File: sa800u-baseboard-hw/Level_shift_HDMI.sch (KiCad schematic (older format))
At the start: 6 parts

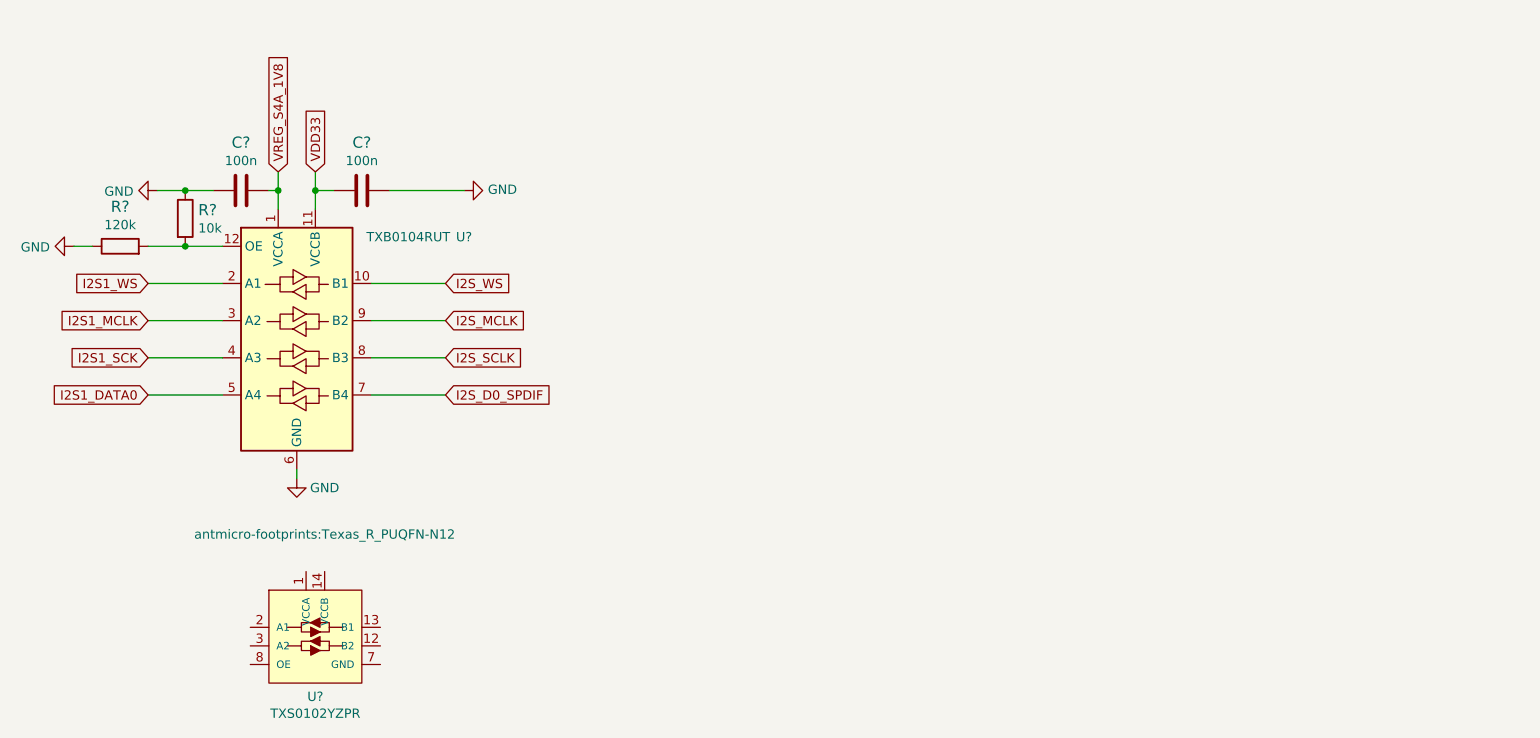
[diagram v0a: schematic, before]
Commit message: added level shifters for I2S, reset, I2C, and GPIO
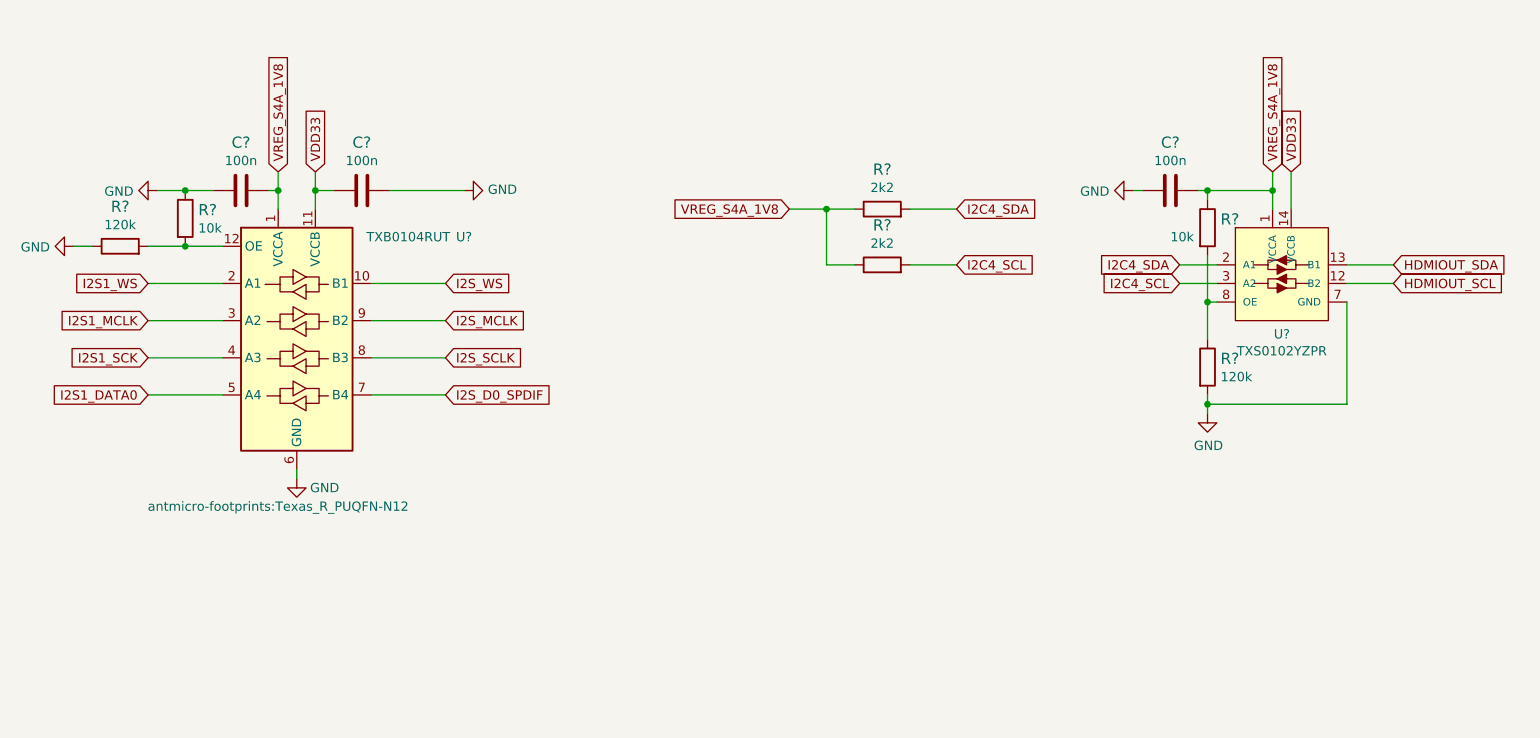
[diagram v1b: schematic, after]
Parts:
- added C?: C_100n_0402, antmicro-footprints:0402-cap, symbol antmicroCapacitors0402:C_100n_0402
- added R?: R_10k_0603, antmicro-footprints:0603-res, symbol antmicroResistors0603:R_10k_0603
- added R?: R_120k_0402, antmicro-footprints:0402-res, symbol antmicroResistors0402:R_120k_0402
- added R? (x2): R_2k2_0402, antmicro-footprints:0402-res, symbol antmicroResistors0402:R_2k2_0402
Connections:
- net GND: now also U?.7 (GND), C?.2, R?.2
- net VDD33: now also U?.14 (VCCB)
- net VREG_S4A_1V8: now also U?.1 (VCCA), C?.1, R?.1, R?.1, R?.1
- net HDMIOUT_SCL: now reaches U?.12 (B2)
- net HDMIOUT_SDA: now reaches U?.13 (B1)
- net I2C4_SDA: now reaches U?.2 (A1)
- net I2C4_SDA: now also R?.2
- net I2C4_SCL: now reaches U?.3 (A2)
- net I2C4_SCL: now also R?.2
- net at U?.8 (OE): now also R?.1, R?.2
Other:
- moved on the sheet: U?
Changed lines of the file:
@@
 F 0 "U?" H 4650 3100 50  0000 C CNN
 F 1 "TXB0104RUT" H 4350 3100 50  0000 C CNN
-F 2 "antmicro-footprints:Texas_R_PUQFN-N12" H 3900 1500 50  0000 C CNN
+F 2 "antmicro-footprints:Texas_R_PUQFN-N12" H 3650 1650 50  0000 C CNN
 F 3 "http://www.ti.com/lit/ds/symlink/txb0104.pdf" H 3860 2645 50  0001 C CNN
 F 4 "Texas Instruments" H 3350 1700 50  0001 C CNN "Manufacturer"
@@
 L HDMI:TXS0102YZPR U?
 U 1 1 61AE6E30
-P 3600 3900
-F 0 "U?" H 3850 3327 50  0000 C CNN
-F 1 "TXS0102YZPR" H 3850 3236 50  0000 C CNN
-F 2 "" H 3050 4100 50  0001 C CNN
-F 3 "" H 3050 4100 50  0001 C CNN
-	1    3600 3900
+P 8800 1950
+F 0 "U?" H 9050 1377 50  0000 C CNN
+F 1 "TXS0102YZPR" H 9050 1286 50  0000 C CNN
+F 2 "" H 8250 2150 50  0001 C CNN
+F 3 "" H 8250 2150 50  0001 C CNN
+	1    8800 1950
 	1    0    0    -1
 $EndComp
@@
 Wire Wire Line
 	3750 3300 3750 3250
+Text GLabel 8500 2250 0    50   Input ~ 0
+I2C4_SCL
+Text GLabel 9650 2250 2    50   Input ~ 0
+HDMIOUT_SCL
+Text GLabel 8500 2150 0    50   Input ~ 0
+I2C4_SDA
+Text GLabel 9650 2150 2    50   Input ~ 0
+HDMIOUT_SDA
+Wire Wire Line
+	8700 2150 8500 2150
+Wire Wire Line
+	8500 2250 8700 2250
+Wire Wire Line
+	9400 2150 9650 2150
+Wire Wire Line
+	9400 2250 9650 2250
+Text GLabel 9000 1650 1    50   Input ~ 0
+VREG_S4A_1V8
+Text GLabel 9100 1650 1    50   Input ~ 0
+VDD33
+Wire Wire Line
+	9000 1650 9000 1750
+Wire Wire Line
+	9100 1650 9100 1850
+Wire Wire Line
+	9000 1750 8650 1750
+Connection ~ 9000 1750
+Wire Wire Line
+	9000 1750 9000 1850
+$Comp
+L antmicroCapacitors0402:C_100n_0402 C?
+U 1 1 61B0A89F
+P 8450 1750
+F 0 "C?" V 8192 1750 60  0000 C CNN
+F 1 "C_100n_0402" H 8450 1600 60  0001 C CNN
+F 2 "antmicro-footprints:0402-cap" H 8650 1950 60  0001 L CNN
+F 3 "" H 8450 1750 50  0001 C CNN
+F 4 "Walsin" H 8650 2150 60  0001 L CNN "Manufacturer"
+F 5 "0402X104K6R3CT" H 8650 2050 60  0001 L CNN "MPN"
+F 6 "100n" V 8290 1750 50  0000 C CNN "Val"
+	1    8450 1750
+	0    1    1    0
+$EndComp
+Wire Wire Line
+	8300 1750 8250 1750
+$Comp
+L power:GND #PWR?
+U 1 1 61B0B3E9
+P 8250 1750
+F 0 "#PWR?" H 8250 1500 50  0001 C CNN
+F 1 "GND" V 8255 1622 50  0000 R CNN
+F 2 "" H 8250 1750 50  0001 C CNN
+F 3 "" H 8250 1750 50  0001 C CNN
+	1    8250 1750
+	0    1    1    0
+$EndComp
+Wire Wire Line
+	8650 1750 8650 1800
+Wire Wire Line
+	8650 2350 8700 2350
+Connection ~ 8650 1750
+Wire Wire Line
+	8650 1750 8600 1750
+Wire Wire Line
+	8650 2350 8650 2550
+Connection ~ 8650 2350
+$Comp
+L antmicroResistors0603:R_10k_0603 R?
+U 1 1 61B0D538
+P 8650 1950
+F 0 "R?" V 8605 2020 60  0000 L CNN
+F 1 "R_10k_0603" H 8650 1800 60  0001 C CNN
+F 2 "antmicro-footprints:0603-res" H 8850 2150 60  0001 L CNN
+F 3 "" H 8650 1950 50  0001 C CNN
+F 4 "BOURNS" H 8850 2350 60  0001 L CNN "Manufacturer"
+F 5 "CR0603-JW-103ELF" H 8850 2250 60  0001 L CNN "MPN"
+F 6 "10k" V 8700 1750 50  0000 L CNN "Val"
+	1    8650 1950
+	0    1    1    0
+$EndComp
+Wire Wire Line
+	8650 2100 8650 2350
+$Comp
+L antmicroResistors0402:R_120k_0402 R?
+U 1 1 61B0E0A9
+P 8650 2700
+F 0 "R?" V 8605 2770 60  0000 L CNN
+F 1 "R_120k_0402" H 8650 2550 60  0001 C CNN
+F 2 "antmicro-footprints:0402-res" H 8850 2900 60  0001 L CNN
+F 3 "" H 8650 2700 50  0001 C CNN
+F 4 "VISHAY" H 8850 3100 60  0001 L CNN "Manufacturer"
+F 5 "CRCW0402120KFKED" H 8850 3000 60  0001 L CNN "MPN"
+F 6 "120k" V 8703 2770 50  0000 L CNN "Val"
+	1    8650 2700
+	0    1    1    0
+$EndComp
+$Comp
+L power:GND #PWR?
+U 1 1 61B0EB2E
+P 8650 2950
+F 0 "#PWR?" H 8650 2700 50  0001 C CNN
+F 1 "GND" H 8655 2777 50  0000 C CNN
+F 2 "" H 8650 2950 50  0001 C CNN
+F 3 "" H 8650 2950 50  0001 C CNN
+	1    8650 2950
+	1    0    0    -1
+$EndComp
+Wire Wire Line
+	8650 2950 8650 2900
+Wire Wire Line
+	9400 2350 9400 2900
+Wire Wire Line
+	9400 2900 8650 2900
+Connection ~ 8650 2900
+Wire Wire Line
+	8650 2900 8650 2850
+$Comp
+L antmicroResistors0402:R_2k2_0402 R?
+U 1 1 61B1457B
+P 6900 1850
+F 0 "R?" H 6900 2063 60  0000 C CNN
+F 1 "R_2k2_0402" H 6900 1700 60  0001 C CNN
+F 2 "antmicro-footprints:0402-res" H 7100 2050 60  0001 L CNN
+F 3 "" H 6900 1850 50  0001 C CNN
+F 4 "YAGEO" H 7100 2250 60  0001 L CNN "Manufacturer"
+F 5 "RC0402FR-072K2L" H 7100 2150 60  0001 L CNN "MPN"
+F 6 "2k2" H 6900 1965 50  0000 C CNN "Val"
+	1    6900 1850
+	1    0    0    -1
+$EndComp
+$Comp
+L antmicroResistors0402:R_2k2_0402 R?
+U 1 1 61B14A5A
+P 6900 2150
+F 0 "R?" H 6900 2363 60  0000 C CNN
+F 1 "R_2k2_0402" H 6900 2000 60  0001 C CNN
+F 2 "antmicro-footprints:0402-res" H 7100 2350 60  0001 L CNN
+F 3 "" H 6900 2150 50  0001 C CNN
+F 4 "YAGEO" H 7100 2550 60  0001 L CNN "Manufacturer"
+F 5 "RC0402FR-072K2L" H 7100 2450 60  0001 L CNN "MPN"
+F 6 "2k2" H 6900 2265 50  0000 C CNN "Val"
+	1    6900 2150
+	1    0    0    -1
+$EndComp
+Wire Wire Line
+	6750 1850 6600 1850
+Wire Wire Line
+	6750 2150 6600 2150
+Wire Wire Line
+	6600 2150 6600 1850
+Connection ~ 6600 1850
+Wire Wire Line
+	6600 1850 6400 1850
+Text GLabel 6400 1850 0    50   Input ~ 0
+VREG_S4A_1V8
+Text GLabel 7300 1850 2    50   Input ~ 0
+I2C4_SDA
+Text GLabel 7300 2150 2    50   Input ~ 0
+I2C4_SCL
+Wire Wire Line
+	7050 1850 7300 1850
+Wire Wire Line
+	7050 2150 7300 2150
 $EndSCHEMATC

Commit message: Review - Add geeral remarks
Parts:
- gave numbers to parts that had none: 11
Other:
- note added: "REMARK:Please unify convention of naming power supply labels.\nWe often use global labels. Always check that the name is exactly the same."
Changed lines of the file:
@@
 $EndDescr
 $Comp
-L antmicroLogicTranslatorsLevelShifters:TXB0104RUT U?
+L antmicroLogicTranslatorsLevelShifters:TXB0104RUT U5
 U 1 1 61AD2A25
 P 3750 2550
-F 0 "U?" H 4650 3100 50  0000 C CNN
+F 0 "U5" H 4650 3100 50  0000 C CNN
 F 1 "TXB0104RUT" H 4350 3100 50  0000 C CNN
 F 2 "antmicro-footprints:Texas_R_PUQFN-N12" H 3650 1650 50  0000 C CNN
@@
 I2S1_DATA0
 $Comp
-L HDMI:TXS0102YZPR U?
+L HDMI:TXS0102YZPR U6
 U 1 1 61AE6E30
 P 8800 1950
-F 0 "U?" H 9050 1377 50  0000 C CNN
+F 0 "U6" H 9050 1377 50  0000 C CNN
 F 1 "TXS0102YZPR" H 9050 1286 50  0000 C CNN
 F 2 "" H 8250 2150 50  0001 C CNN
@@
 	4150 2250 4550 2250
 $Comp
-L power:GND #PWR?
+L power:GND #PWR0119
 U 1 1 61AEC03D
 P 3000 1750
-F 0 "#PWR?" H 3000 1500 50  0001 C CNN
+F 0 "#PWR0119" H 3000 1500 50  0001 C CNN
 F 1 "GND" V 3005 1622 50  0000 R CNN
 F 2 "" H 3000 1750 50  0001 C CNN
@@
 	3650 1750 3650 1850
 $Comp
-L power:GND #PWR?
+L power:GND #PWR0120
 U 1 1 61AEC562
 P 4650 1750
-F 0 "#PWR?" H 4650 1500 50  0001 C CNN
+F 0 "#PWR0120" H 4650 1500 50  0001 C CNN
 F 1 "GND" V 4655 1622 50  0000 R CNN
 F 2 "" H 4650 1750 50  0001 C CNN
@@
 	3850 1750 3850 1850
 $Comp
-L antmicroCapacitors0402:C_100n_0402 C?
+L antmicroCapacitors0402:C_100n_0402 C34
 U 1 1 61AEDF92
 P 3450 1750
-F 0 "C?" V 3192 1750 60  0000 C CNN
+F 0 "C34" V 3192 1750 60  0000 C CNN
 F 1 "C_100n_0402" H 3450 1600 60  0001 C CNN
 F 2 "antmicro-footprints:0402-cap" H 3650 1950 60  0001 L CNN
@@
 	3600 1750 3650 1750
 $Comp
-L antmicroCapacitors0402:C_100n_0402 C?
+L antmicroCapacitors0402:C_100n_0402 C35
 U 1 1 61AEE5E6
 P 4100 1750
-F 0 "C?" V 3842 1750 60  0000 C CNN
+F 0 "C35" V 3842 1750 60  0000 C CNN
 F 1 "C_100n_0402" H 4100 1600 60  0001 C CNN
 F 2 "antmicro-footprints:0402-cap" H 4300 1950 60  0001 L CNN
@@
 	3350 2050 3150 2050
 $Comp
-L antmicroResistors0603:R_10k_0603 R?
+L antmicroResistors0603:R_10k_0603 R45
 U 1 1 61AF1E74
 P 3150 1900
-F 0 "R?" V 3105 1970 60  0000 L CNN
+F 0 "R45" V 3105 1970 60  0000 L CNN
 F 1 "R_10k_0603" H 3150 1750 60  0001 C CNN
 F 2 "antmicro-footprints:0603-res" H 3350 2100 60  0001 L CNN
@@
 	3150 2050 2950 2050
 $Comp
-L antmicroResistors0402:R_120k_0402 R?
+L antmicroResistors0402:R_120k_0402 R44
 U 1 1 61AF2C4D
 P 2800 2050
-F 0 "R?" H 2800 2263 60  0000 C CNN
+F 0 "R44" H 2800 2263 60  0000 C CNN
 F 1 "R_120k_0402" H 2800 1900 60  0001 C CNN
 F 2 "antmicro-footprints:0402-res" H 3000 2250 60  0001 L CNN
@@
 $EndComp
 $Comp
-L power:GND #PWR?
+L power:GND #PWR0121
 U 1 1 61AF30FD
 P 2550 2050
-F 0 "#PWR?" H 2550 1800 50  0001 C CNN
+F 0 "#PWR0121" H 2550 1800 50  0001 C CNN
 F 1 "GND" V 2555 1922 50  0000 R CNN
 F 2 "" H 2550 2050 50  0001 C CNN
@@
 	2550 2050 2650 2050
 $Comp
-L power:GND #PWR?
+L power:GND #PWR0122
 U 1 1 61AF391A
 P 3750 3300
-F 0 "#PWR?" H 3750 3050 50  0001 C CNN
+F 0 "#PWR0122" H 3750 3050 50  0001 C CNN
 F 1 "GND" H 3900 3250 50  0000 C CNN
 F 2 "" H 3750 3300 50  0001 C CNN
@@
 	9000 1750 9000 1850
 $Comp
-L antmicroCapacitors0402:C_100n_0402 C?
+L antmicroCapacitors0402:C_100n_0402 C36
 U 1 1 61B0A89F
 P 8450 1750
-F 0 "C?" V 8192 1750 60  0000 C CNN
+F 0 "C36" V 8192 1750 60  0000 C CNN
 F 1 "C_100n_0402" H 8450 1600 60  0001 C CNN
 F 2 "antmicro-footprints:0402-cap" H 8650 1950 60  0001 L CNN
@@
 	8300 1750 8250 1750
 $Comp
-L power:GND #PWR?
+L power:GND #PWR0123
 U 1 1 61B0B3E9
 P 8250 1750
-F 0 "#PWR?" H 8250 1500 50  0001 C CNN
+F 0 "#PWR0123" H 8250 1500 50  0001 C CNN
 F 1 "GND" V 8255 1622 50  0000 R CNN
 F 2 "" H 8250 1750 50  0001 C CNN
@@
 Connection ~ 8650 2350
 $Comp
-L antmicroResistors0603:R_10k_0603 R?
+L antmicroResistors0603:R_10k_0603 R48
 U 1 1 61B0D538
 P 8650 1950
-F 0 "R?" V 8605 2020 60  0000 L CNN
+F 0 "R48" V 8605 2020 60  0000 L CNN
 F 1 "R_10k_0603" H 8650 1800 60  0001 C CNN
 F 2 "antmicro-footprints:0603-res" H 8850 2150 60  0001 L CNN
@@
 	8650 2100 8650 2350
 $Comp
-L antmicroResistors0402:R_120k_0402 R?
+L antmicroResistors0402:R_120k_0402 R49
 U 1 1 61B0E0A9
 P 8650 2700
-F 0 "R?" V 8605 2770 60  0000 L CNN
+F 0 "R49" V 8605 2770 60  0000 L CNN
 F 1 "R_120k_0402" H 8650 2550 60  0001 C CNN
 F 2 "antmicro-footprints:0402-res" H 8850 2900 60  0001 L CNN
@@
 $EndComp
 $Comp
-L power:GND #PWR?
+L power:GND #PWR0124
 U 1 1 61B0EB2E
 P 8650 2950
-F 0 "#PWR?" H 8650 2700 50  0001 C CNN
+F 0 "#PWR0124" H 8650 2700 50  0001 C CNN
 F 1 "GND" H 8655 2777 50  0000 C CNN
 F 2 "" H 8650 2950 50  0001 C CNN
@@
 	8650 2900 8650 2850
 $Comp
-L antmicroResistors0402:R_2k2_0402 R?
+L antmicroResistors0402:R_2k2_0402 R46
 U 1 1 61B1457B
 P 6900 1850
-F 0 "R?" H 6900 2063 60  0000 C CNN
+F 0 "R46" H 6900 2063 60  0000 C CNN
 F 1 "R_2k2_0402" H 6900 1700 60  0001 C CNN
 F 2 "antmicro-footprints:0402-res" H 7100 2050 60  0001 L CNN
@@
 $EndComp
 $Comp
-L antmicroResistors0402:R_2k2_0402 R?
+L antmicroResistors0402:R_2k2_0402 R47
 U 1 1 61B14A5A
 P 6900 2150
-F 0 "R?" H 6900 2363 60  0000 C CNN
+F 0 "R47" H 6900 2363 60  0000 C CNN
 F 1 "R_2k2_0402" H 6900 2000 60  0001 C CNN
 F 2 "antmicro-footprints:0402-res" H 7100 2350 60  0001 L CNN
@@
 Wire Wire Line
 	7050 2150 7300 2150
+Text Notes 3650 975  0    50   ~ 0
+REMARK:Please unify convention of naming power supply labels.\nWe often use global labels. Always check that the name is exactly the same.
 $EndSCHEMATC

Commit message: introducing minor genreal improvements
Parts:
- removed U6: TXS0102YZPR, symbol HDMI:TXS0102YZPR
- added U?: TXS0102YZPR, antmicro-footprints:BGA8C50P2X4_88X188X50N, symbol antmicroLogicTranslatorsLevelShifters:TXS0102YZPR
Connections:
- net GND: now also U?.7 (GND)
- net HDMIOUT_SCL: now also U?.12 (B2)
- net HDMIOUT_SDA: now also U?.13 (B1)
- net I2C4_SCL: now also U?.3 (A2)
- net I2C4_SDA: now also U?.2 (A1)
- net VDD33: now also U?.14 (VCCB)
- net VREG_S4A_1V8: now also U?.1 (VCCA)
- net at R48.2, R49.1: now also U?.8 (OE)
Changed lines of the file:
@@
 Text GLabel 2950 2850 0    50   Input ~ 0
 I2S1_DATA0
-$Comp
-L HDMI:TXS0102YZPR U6
-U 1 1 61AE6E30
-P 8800 1950
-F 0 "U6" H 9050 1377 50  0000 C CNN
-F 1 "TXS0102YZPR" H 9050 1286 50  0000 C CNN
-F 2 "" H 8250 2150 50  0001 C CNN
-F 3 "" H 8250 2150 50  0001 C CNN
-	1    8800 1950
-	1    0    0    -1
-$EndComp
 Text GLabel 3850 1650 1    50   Input ~ 0
 VDD33
@@
 Text Notes 3650 975  0    50   ~ 0
 REMARK:Please unify convention of naming power supply labels.\nWe often use global labels. Always check that the name is exactly the same.
+$Comp
+L antmicroLogicTranslatorsLevelShifters:TXS0102YZPR U?
+U 1 1 61A10975
+P 8800 1950
+F 0 "U?" H 9050 1377 50  0000 C CNN
+F 1 "TXS0102YZPR" H 9050 1286 50  0000 C CNN
+F 2 "antmicro-footprints:BGA8C50P2X4_88X188X50N" H 8800 1950 50  0001 C CNN
+F 3 "https://www.ti.com/lit/ds/symlink/txs0102.pdf?ts=1637914596981&ref_url=https%253A%252F%252Fwww.ti.com%252Fstore%252Fti%252Fen%252Fp%252Fproduct%252F%253Fp%253DTXS0102DCTR%2526keyMatch%253DTXS0102DCTR%2526tisearch%253Dsearch-everything%2526usecase%253DOPN" H 8800 1950 50  0001 C CNN
+F 4 "TXS0102YZPR" H 9050 1195 50  0000 C CNN "MPN"
+F 5 "Texas Instruments" H 9050 1104 50  0000 C CNN "Manufacturer"
+	1    8800 1950
+	1    0    0    -1
+$EndComp
 $EndSCHEMATC
